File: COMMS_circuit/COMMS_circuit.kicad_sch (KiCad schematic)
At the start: 2 parts, among them X1 SIT8918AE-13-33N-45, X2 SIT8925BA-78-25N-125.000000

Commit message: Changes I missed cause id been staring at it to long
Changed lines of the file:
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@@
 	(generator "eeschema")
 	(generator_version "8.0")
-	(paper "A4")
+	(paper "A")
 	(no_connect
 		(at 160.02 27.94)
@@
 	(polyline
 		(pts
-			(xy 202.184 49.022) (xy 202.184 86.106)
+			(xy 201.93 49.022) (xy 201.93 87.63)
 		)
 		(stroke
@@
 	(polyline
 		(pts
-			(xy 202.184 86.106) (xy 123.19 86.614)
+			(xy 201.93 87.63) (xy 122.936 87.63)
 		)
 		(stroke
@@
 	(text "Peripherals"
 		(exclude_from_sim no)
-		(at 145.034 82.55 0)
+		(at 144.526 83.058 0)
 		(effects
 			(font
@@
 	)
 	(sheet
-		(at 92.456 104.902)
+		(at 88.9 104.394)
 		(size 25.4 25.908)
 		(stroke
@@
 		)
 		(property "Sheetname" "Power"
-			(at 102.108 117.348 0)
+			(at 98.552 116.84 0)
 			(effects
 				(font
@@
 		)
 		(property "Sheetfile" "Power.kicad_sch"
-			(at 96.52 119.888 0)
-			(effects
-				(font
+			(at 92.964 119.38 0)
+			(effects
+				(font

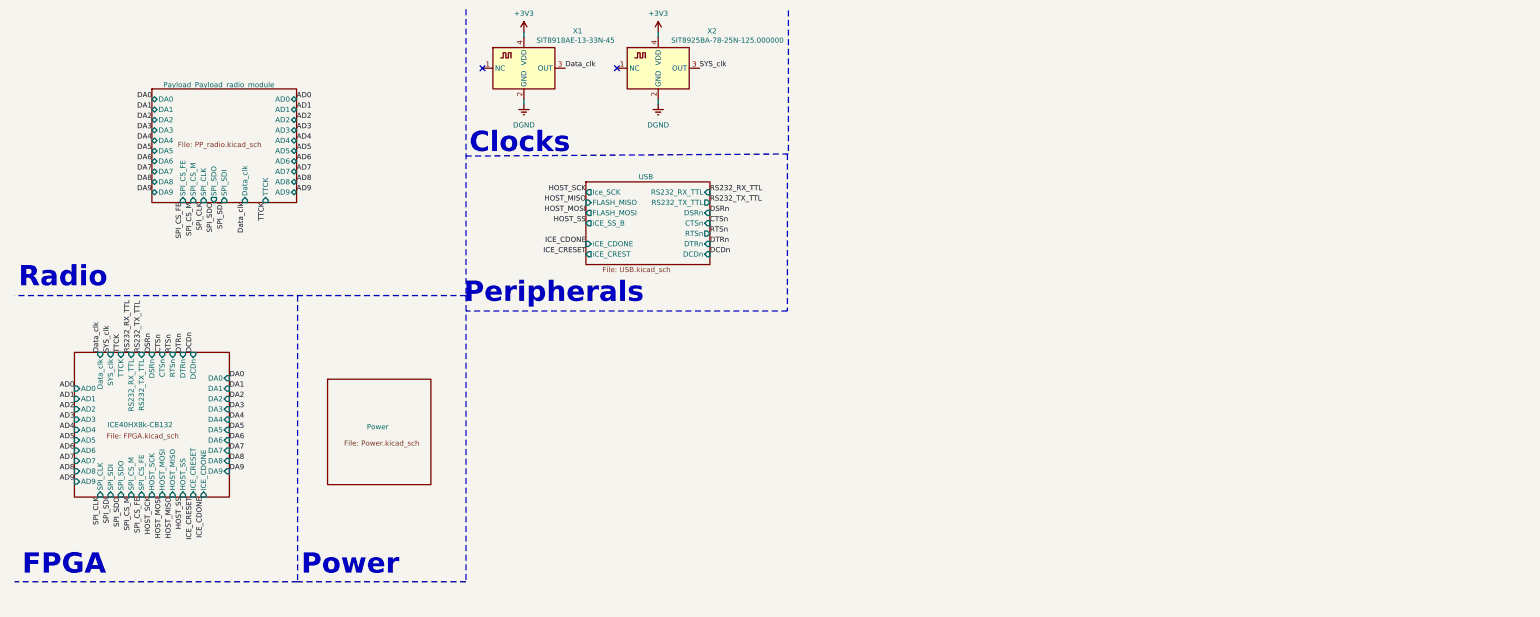
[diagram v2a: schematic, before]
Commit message: Stick a RP2040 on the side and see if we can program an FPGA with it
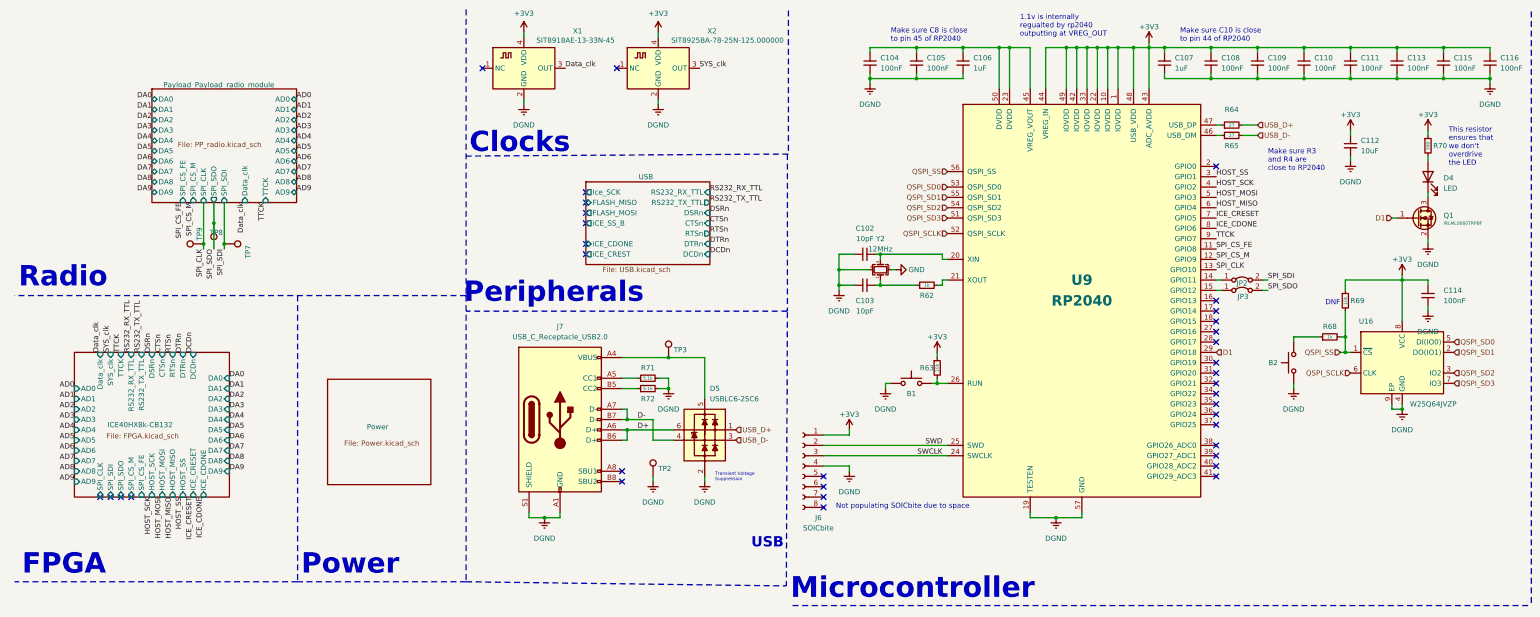
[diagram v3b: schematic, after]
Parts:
- added B1, B2: KMR2, Button_Switch_SMD:SW_Push_1P1T_NO_CK_KMR2, symbol Switch:SW_Push
- added C102, C103: 10pF, Capacitor_SMD:C_0603_1608Metric, symbol Device:C_Small
- added C104, C105, C108, C109, C110, C111, C113, C114, C115, C116: 100nF, Capacitor_SMD:C_0603_1608Metric, symbol Device:C_Small
- added C106, C107: 1uF, Capacitor_SMD:C_0603_1608Metric, symbol Device:C_Small
- added C112: 10uF, Capacitor_SMD:C_0603_1608Metric, symbol Device:C_Small
- added D4: LED, Diode_SMD:D_0603_1608Metric_Pad1.05x0.95mm_HandSolder, symbol Device:LED
- added D5: USBLC6-2SC6, Package_TO_SOT_SMD:TSOT-23-6_HandSoldering, symbol Diode_TVS_AKL:USBLC6-2SC6
- added J6: SOICbite, BPP_Lib:SOIC_clipProgSmall, symbol Connector:Conn_01x08_Female
- added J7: USB_C_Receptacle_USB2.0, Connector_USB:USB_C_Receptacle_GCT_USB4105-xx-A_16P_TopMnt_Horizontal, symbol Connector:USB_C_Receptacle_USB2.0
- added JP2, JP3: Jumper_2_Bridged, Jumper:SolderJumper-2_P1.3mm_Bridged2Bar_Pad1.0x1.5mm, symbol Jumper:Jumper_2_Bridged
- added Q1: IRLML0060TRPBF, Package_TO_SOT_SMD:SOT-23-3, symbol Device:Q_NMOS_GSD
- added R62, R68: 1k, Resistor_SMD:R_0603_1608Metric, symbol Device:R_Small
- added R63, R69: 10k, Resistor_SMD:R_0603_1608Metric, symbol Device:R_Small
- added R64, R65: 27, Resistor_SMD:R_0603_1608Metric, symbol Device:R_Small
- added R70: 590, Resistor_SMD:R_0603_1608Metric, symbol Device:R_Small
- added R71, R72: 5.1k, Resistor_SMD:R_0603_1608Metric, symbol Device:R_Small
- added TP2, TP3, TP7, TP8, TP9: TestPoint, TestPoint:TestPoint_Keystone_5000-5004_Miniature, symbol Connector:TestPoint
- added U16: W25Q64JVZP, Package_SON:WSON-8-1EP_6x5mm_P1.27mm_EP3.4x4.3mm, symbol Memory_Flash:W25Q128JVS
- added U9: RP2040, BPP_Lib:RP2040-QFN-56, symbol MCU_RaspberryPi:RP2040
- added Y2: 12MHz, Crystal:Crystal_SMD_2520-4Pin_2.5x2.0mm, symbol Device:Crystal_GND24_Small
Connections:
- net +3V3: now also C107.1, C108.1, C109.1, C110.1, C111.1, C112.1, C113.1, C114.1, C115.1, C116.1, J6.1 (Pin_1), R63.1, R69.1, R70.1, U16.8 (VCC), U9.1 (IOVDD), U9.10 (IOVDD), U9.22 (IOVDD), U9.33 (IOVDD), U9.42 (IOVDD), U9.43 (ADC_AVDD), U9.44 (VREG_IN), U9.48 (USB_VDD), U9.49 (IOVDD)
- net DGND: now also B1.1, B2.1, C102.1, C103.1, C104.2, C105.2, C106.2, C107.2, C108.2, C109.2, C110.2, C111.2, C112.2, C113.2, C114.2, C115.2, C116.2, D5.2 (VN), J6.4 (Pin_4), J7.A1 (GND), J7.A12 (GND), J7.B1 (GND), J7.B12 (GND), J7.S1 (SHIELD), Q1.2 (S), R71.2, R72.2, TP2.1, U16.4 (GND), U16.9 (EP), U9.19 (TESTEN), U9.57 (GND), Y2.4
- net HOST_MISO: now also U9.6 (GPIO4)
- net HOST_MOSI: now also U9.5 (GPIO3)
- net HOST_SCK: now also U9.4 (GPIO2)
- net HOST_SS: now also U9.3 (GPIO1)
- net ICE_CDONE: now also U9.8 (GPIO6)
- net ICE_CRESET: now also U9.7 (GPIO5)
- net SPI_CLK: now also TP9.1, U9.13 (GPIO10)
- net SPI_CS_FE: now also U9.11 (GPIO8)
- net SPI_CS_M: now also U9.12 (GPIO9)
- net SPI_SDI: now also JP2.2 (B), TP7.1
- net SPI_SDO: now also JP3.2 (B), TP8.1
- net TTCK: now also U9.9 (GPIO7)
- new net: D4.1 (K), Q1.3 (D)
- new net: D4.2 (A), R70.2
- new net: JP2.1 (A), U9.14 (GPIO11)
- new net: JP3.1 (A), U9.15 (GPIO12)
- new net: C102.2, U9.20 (XIN), Y2.3
- new net: R62.2, U9.21 (XOUT)
- new net: C104.1, C105.1, C106.1, U9.23 (DVDD), U9.45 (VREG_VOUT), U9.50 (DVDD)
- new net: B1.2, R63.2, U9.26 (RUN)
- new net: R65.1, U9.46 (USB_DM)
- new net: R64.1, U9.47 (USB_DP)
- new net: D5.5 (VP), J7.A4 (VBUS), J7.A9 (VBUS), J7.B4 (VBUS), J7.B9 (VBUS), TP3.1
- new net: J7.A5 (CC1), R71.1
- new net: J7.B5 (CC2), R72.1
- new net: C103.2, R62.1, Y2.1
- new net: B2.2, R68.1
- new net D+: D5.6 (L1), J7.A6 (D+), J7.B6 (D+)
- new net D-: D5.4 (L2), J7.A7 (D-), J7.B7 (D-)
- new net D1: Q1.1 (G), U9.29 (GPIO18)
- new net GND: Y2.2
- new net QSPI_SCLK: U16.6 (CLK), U9.52 (QSPI_SCLK)
- new net QSPI_SD0: U16.5 (DI(IO0)), U9.53 (QSPI_SD0)
- new net QSPI_SD1: U16.2 (DO(IO1)), U9.55 (QSPI_SD1)
- new net QSPI_SD2: U16.3 (IO2), U9.54 (QSPI_SD2)
- new net QSPI_SD3: U16.7 (IO3), U9.51 (QSPI_SD3)
- new net QSPI_SS: R68.2, R69.2, U16.1 (~{CS}), U9.56 (QSPI_SS)
- new net SWCLK: J6.3 (Pin_3), U9.24 (SWCLK)
- new net SWD: J6.2 (Pin_2), U9.25 (SWD)
- new net USB_D+: D5.1 (L1), R64.2
- new net USB_D-: D5.3 (L2), R65.2
- no-connect marks 2 -> 35
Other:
- note added: "1.1v is internally regualted by rp2040 outputting at VREG_OUT"
- note added: "DNF"
- note added: "Make sure C10 is close to pin 44 of RP2040"
- note added: "Make sure C8 is close to pin 45 of RP2040"
- note added: "Make sure R3 and R4 are close to RP2040"
- note added: "Microcontroller"
- note added: "Not populating SOICbite due to space"
- note added: "This resistor ensures that we don't overdrive the LED"
- note added: "Transient Voltage Suppression"
- note added: "USB"

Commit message: switching the VBUS to RP2040 USB cause its more sensical
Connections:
- net VBUS: now reaches D5.5 (VP), J7.A4 (VBUS), J7.A9 (VBUS), J7.B4 (VBUS), J7.B9 (VBUS), TP3.1
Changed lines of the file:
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@@
 	)
 	(junction
+		(at 181.61 99.06)
+		(diameter 0)
+		(color 0 0 0 0)
+	)
+	(junction
 		(at 317.5 30.48)
 		(diameter 0)
@@
 					(unit 1)
 				)
+			)
+		)
+	)
+	(symbol
+		(lib_id "power:VBUS")
+		(at 181.61 99.06 0)
+		(unit 1)
+		(exclude_from_sim no)
+		(in_bom yes)
+		(on_board yes)
+		(dnp no)
+		(fields_autoplaced yes)
+		(property "Reference" "#PWR084"
+			(at 181.61 102.87 0)
+			(effects
+				(font
+					(size 1.27 1.27)
+				)
+				(hide yes)
+			)
+		)
+		(property "Value" "VBUS"
+			(at 181.61 93.98 0)
+			(effects
+				(font
+					(size 1.27 1.27)
+				)
+			)
+		)
+		(property "Footprint" ""
+			(at 181.61 99.06 0)
+			(effects
+				(font
+					(size 1.27 1.27)
+				)
+				(hide yes)
+			)
+		)
+		(property "Datasheet" ""
+			(at 181.61 99.06 0)
+			(effects
+				(font
+					(size 1.27 1.27)
+				)
+				(hide yes)
+			)
+		)
+		(property "Description" "Power symbol creates a global label with name \"VBUS\""
+			(at 181.61 99.06 0)
+			(effects
+				(font
+					(size 1.27 1.27)
+				)
+				(hide yes)
+			)
+		)
+		(pin "1"
+		)
+		(instances
+			(project "COMMS_circuit"
+				(path "/bdd480c2-e959-4f78-bdcb-24d46c5e40e4"
+					(reference "#PWR084")
+					(unit 1)
+				)
